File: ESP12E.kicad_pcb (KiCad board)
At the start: 2 copper layers, 100 x 100 mm, 55 parts, among them J3 UART, J4 Motor, J5 12v PWR, J6 Sol_1, J7 Sol_2, J8 Sol_3, J9 Sol_4, Q1 IRF520N, Q2 IRF520N, Q3 IRF520N, Q4 IRF520N, Q5 IRF520N, U1 ESP-12E, U2 LM7805_TO220, U3 AMS1117-3.3, U4 HX710(A/B), U5 MPS-2108, U6 MPS-2108, U7 HX710(A/B)

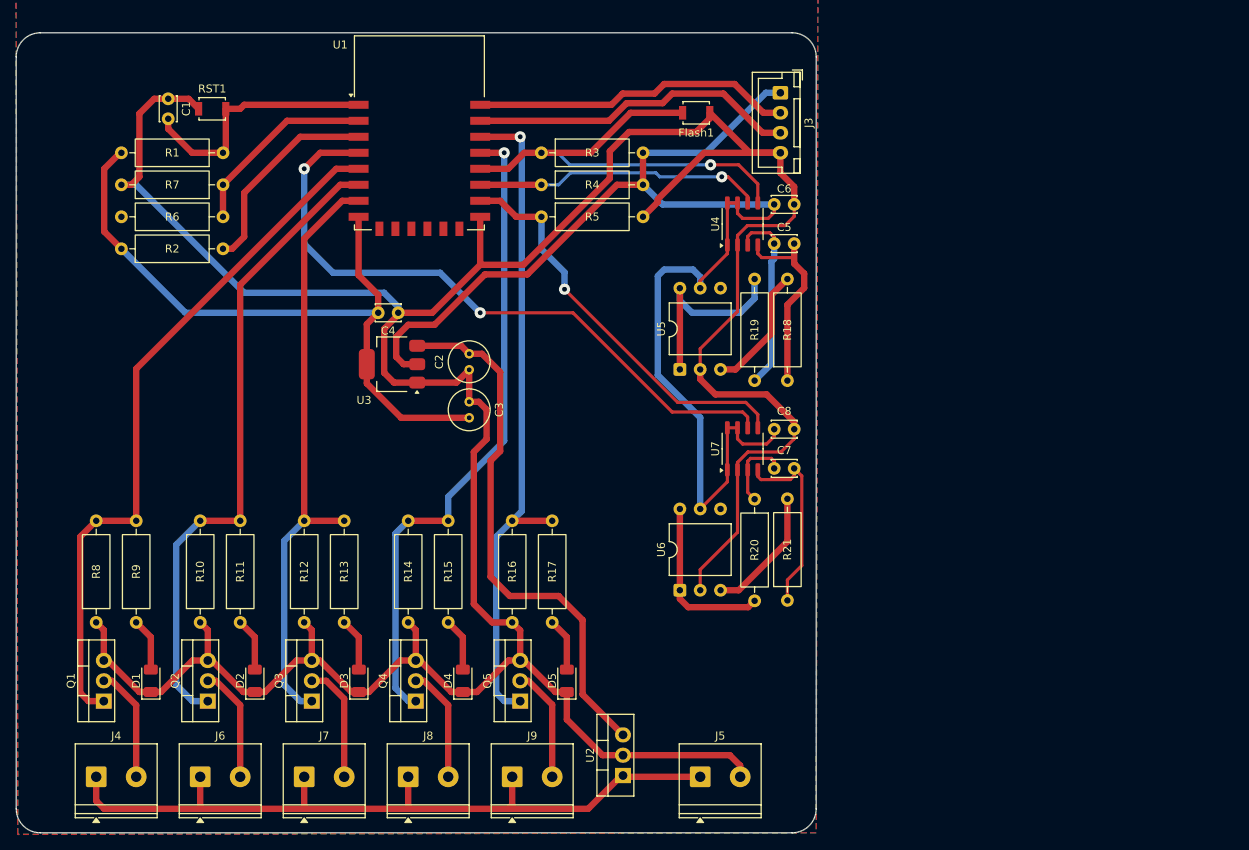
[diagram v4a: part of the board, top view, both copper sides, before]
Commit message: Feat: adding TLP250 for Isolation and driving MOSFETs.
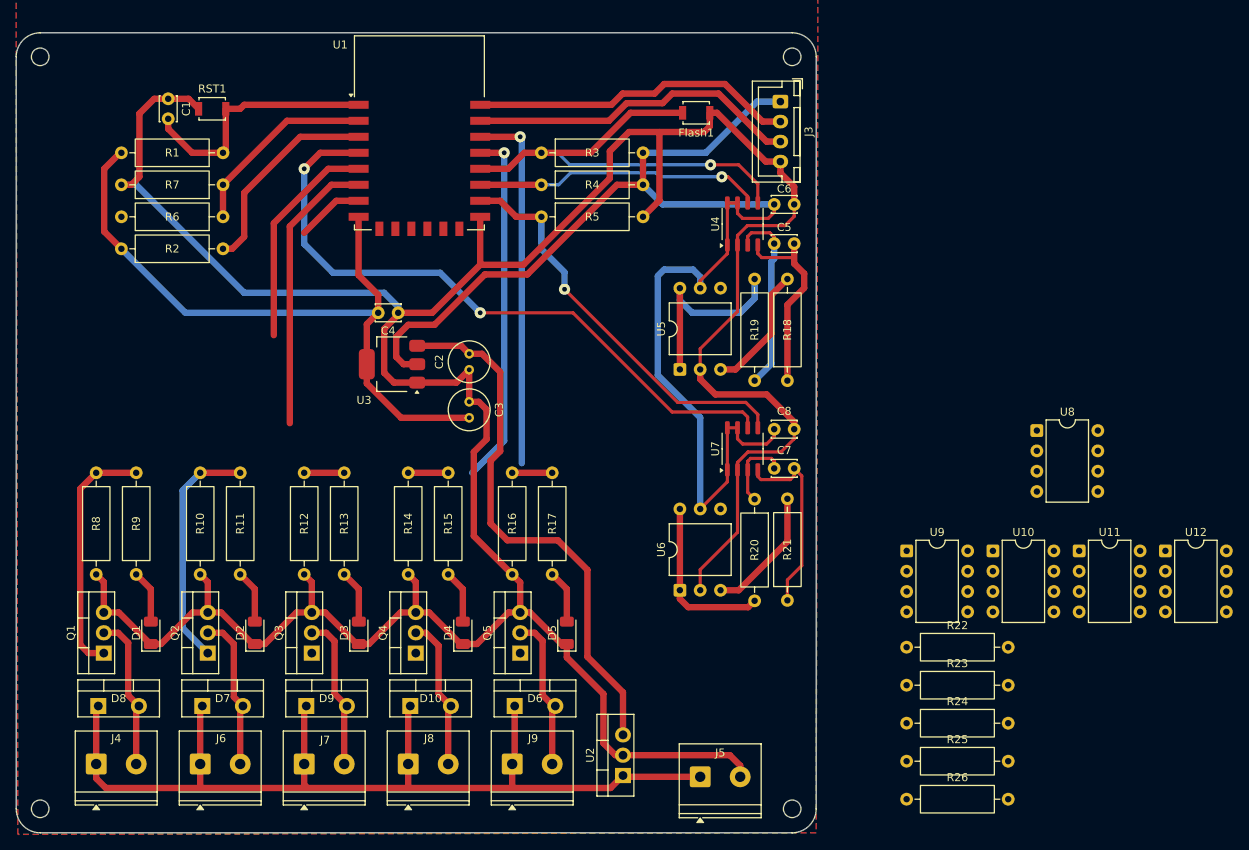
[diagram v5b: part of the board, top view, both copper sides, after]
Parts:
- added D10: MBR745, Package_TO_SOT_THT:TO-220-2_Vertical, F.Cu at (74.3, 104.2)
- added D6: MBR745, Package_TO_SOT_THT:TO-220-2_Vertical, F.Cu at (87.3, 104.2)
- added D7: MBR745, Package_TO_SOT_THT:TO-220-2_Vertical, F.Cu at (48.3, 104.2)
- added D8: MBR745, Package_TO_SOT_THT:TO-220-2_Vertical, F.Cu at (35.3, 104.2)
- added D9: MBR745, Package_TO_SOT_THT:TO-220-2_Vertical, F.Cu at (61.3, 104.2)
- added H1: MountingHole, MountingHole:MountingHole_2.2mm_M2, F.Cu at (122.0, 23.0)
- added H2: MountingHole, MountingHole:MountingHole_2.2mm_M2, F.Cu at (28.0, 23.0)
- added H3: MountingHole, MountingHole:MountingHole_2.2mm_M2, F.Cu at (28.0, 117.0)
- added H4: MountingHole, MountingHole:MountingHole_2.2mm_M2, F.Cu at (122.0, 117.0)
- added R22: 1k, Resistor_THT:R_Axial_DIN0309_L9.0mm_D3.2mm_P12.70mm_Horizontal, F.Cu at (136.3, 96.8)
- added R23: 1k, Resistor_THT:R_Axial_DIN0309_L9.0mm_D3.2mm_P12.70mm_Horizontal, F.Cu at (136.3, 101.5)
- added R24: 1k, Resistor_THT:R_Axial_DIN0309_L9.0mm_D3.2mm_P12.70mm_Horizontal, F.Cu at (136.3, 106.3)
- added R25: 1k, Resistor_THT:R_Axial_DIN0309_L9.0mm_D3.2mm_P12.70mm_Horizontal, F.Cu at (136.3, 111.0)
- added R26: 1k, Resistor_THT:R_Axial_DIN0309_L9.0mm_D3.2mm_P12.70mm_Horizontal, F.Cu at (136.3, 115.8)
- added U10: TLP250, Package_DIP:DIP-8_W7.62mm, F.Cu at (147.1, 84.8)
- added U11: TLP250, Package_DIP:DIP-8_W7.62mm, F.Cu at (157.9, 84.8)
- added U12: TLP250, Package_DIP:DIP-8_W7.62mm, F.Cu at (168.7, 84.8)
- added U8: TLP250, Package_DIP:DIP-8_W7.62mm, F.Cu at (152.6, 69.7)
- added U9: TLP250, Package_DIP:DIP-8_W7.62mm, F.Cu at (136.3, 84.8)
- moved D1 6.00 mm to (41.8, 95.0)
- moved D2 6.00 mm to (54.8, 95.0)
- moved D3 6.00 mm to (67.8, 95.0)
- moved D4 6.00 mm to (80.8, 95.0)
- moved D5 6.00 mm to (93.8, 95.0)
- moved Q1 6.00 mm to (36.0, 97.5)
- moved Q2 6.00 mm to (49.0, 97.5)
- moved Q3 6.00 mm to (62.0, 97.5)
- moved Q4 6.00 mm to (75.0, 97.5)
- moved Q5 6.00 mm to (88.0, 97.5)
- moved R10 6.00 mm to (48.0, 87.7)
- moved R11 6.00 mm to (53.0, 87.7)
- moved R12 6.00 mm to (61.0, 87.7)
- moved R13 6.00 mm to (66.0, 87.7)
- moved R14 6.00 mm to (74.0, 87.7)
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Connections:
- Q1 pad 1: D5/GPIO14/SCLK -> Net-(Q1-G)
- Q2 pad 1: D6/GPIO12/MISO -> Net-(Q2-G)
- Q3 pad 1: D7/GPIO13/MOSI -> Net-(Q3-G)
- Q4 pad 1: D2/SDA/GPIO4 -> Net-(Q4-G)
- Q5 pad 1: D1/SCL/GPIO5 -> Net-(Q5-G)
- R10 pad 2: D6/GPIO12/MISO -> Net-(Q2-G)
- R11 pad 2: D6/GPIO12/MISO -> Net-(Q2-G)
- R12 pad 2: D7/GPIO13/MOSI -> Net-(Q3-G)
- R13 pad 2: D7/GPIO13/MOSI -> Net-(Q3-G)
- R14 pad 2: D2/SDA/GPIO4 -> Net-(Q4-G)
- R15 pad 2: D2/SDA/GPIO4 -> Net-(Q4-G)
- R16 pad 2: D1/SCL/GPIO5 -> Net-(Q5-G)
- R17 pad 2: D1/SCL/GPIO5 -> Net-(Q5-G)
- R8 pad 2: D5/GPIO14/SCLK -> Net-(Q1-G)
- R9 pad 2: D5/GPIO14/SCLK -> Net-(Q1-G)
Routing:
- net D7/GPIO13/MOSI: track 74.8 -> 8.46 mm
- net D5/GPIO14/SCLK: track 87.9 -> 27.4 mm
- net D6/GPIO12/MISO: track 81.0 -> 35.4 mm
- net D1/SCL/GPIO5: track 84.3 -> 45.9 mm
- net D2/SDA/GPIO4: track 81.7 -> 44.7 mm
- net +12V: track 96.8 -> 127.6 mm
- net Net-(Q1-G): track 0.00 -> 30.7 mm
- net Net-(Q2-G): track 0.00 -> 29.8 mm
- net GND: track 413.9 -> 402.2 mm
- net Net-(D6-A): track 14.3 -> 19.6 mm
- net Net-(D7-A): track 14.3 -> 19.4 mm
- net Net-(D8-A): track 14.3 -> 19.4 mm
- net Net-(Q5-G): track 0.00 -> 5.00 mm
- net Net-(Q4-G): track 0.00 -> 5.00 mm
- net Net-(Q3-G): track 0.00 -> 5.00 mm
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
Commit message: working: continue at Work.
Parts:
- J4, J5, J6, J7, J8, J9: footprint TerminalBlock_Phoenix:TerminalBlock_Phoenix_PT-1,5-2-5.0-H_1x02_P5.00mm_Horizontal -> TerminalBlock_RND:TerminalBlock_RND_205-00276_1x02_P5.00mm_Vertical
- R1, R10, R11, R12, R13, R14, R15, R16, R17, R18, R19, R2, R20, R21, R22, R23, R24, R25, R26, R3, R4, R5, R6, R7, R8, R9: footprint Resistor_THT:R_Axial_DIN0309_L9.0mm_D3.2mm_P12.70mm_Horizontal -> Resistor_SMD:R_1206_3216Metric_Pad1.30x1.75mm_HandSolder
- moved U12 135.3 mm to (33.6, 76.6)
- moved R26 112.5 mm to (30.6, 77.5), turned to 90 degrees
- moved U11 111.6 mm to (46.6, 76.6)
- moved R25 98.2 mm to (44.0, 77.5), turned to 90 degrees
- moved U10 87.9 mm to (59.6, 76.6)
- moved R24 84.4 mm to (57.0, 77.5), turned to 90 degrees
- moved R23 70.6 mm to (70.0, 77.5), turned to 90 degrees
- moved U8 67.3 mm to (85.6, 76.6)
- moved U9 64.3 mm to (72.6, 76.6)
- moved R22 56.7 mm to (83.0, 77.5), turned to 90 degrees
- moved Flash1 22.0 mm to (89.2, 37.2)
- moved J3 19.5 mm to (101.8, 23.0), turned to 0 degrees
- moved R2 15.3 mm to (53.5, 31.9), turned to 90 degrees
- moved R18 15.3 mm to (122.4, 48.2)
- moved R19 15.3 mm to (118.3, 48.2)
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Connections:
- J3 pad 1: +3.3V -> TX
- J3 pad 2: TX -> RX
- J3 pad 3: RX -> +3.3V
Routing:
- net +12V: track 127.6 -> 293.7 mm
- net +3.3V: track 251.6 -> 112.8 mm, vias 0 -> 2
- net D0/GPIO16: track 82.9 -> 3.20 mm, vias 2 -> 1
- net D3/GPIO0: track 59.2 -> 8.60 mm, vias 1 -> 0
- net D8/GPIO15/SS: track 51.0 -> 4.66 mm, vias 1 -> 0
- net GND: track 402.2 -> 369.2 mm, vias 0 -> 1
- net D7/GPIO13/MOSI: track 8.46 -> 41.1 mm
- net D4/GPIO2: track 36.1 -> 5.31 mm, vias 1 -> 0
- net D5/GPIO14/SCLK: track 27.4 -> 56.0 mm
- net Net-(U4-INP): track 26.1 -> 0.00 mm
- net Net-(R19-Pad2): track 24.8 -> 0.00 mm
- net Net-(U7-INP): track 24.3 -> 0.00 mm
- net Net-(U4-INN): track 23.7 -> 0.00 mm
- net Net-(R20-Pad2): track 21.3 -> 0.00 mm
- net TX: track 40.5 -> 23.4 mm
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
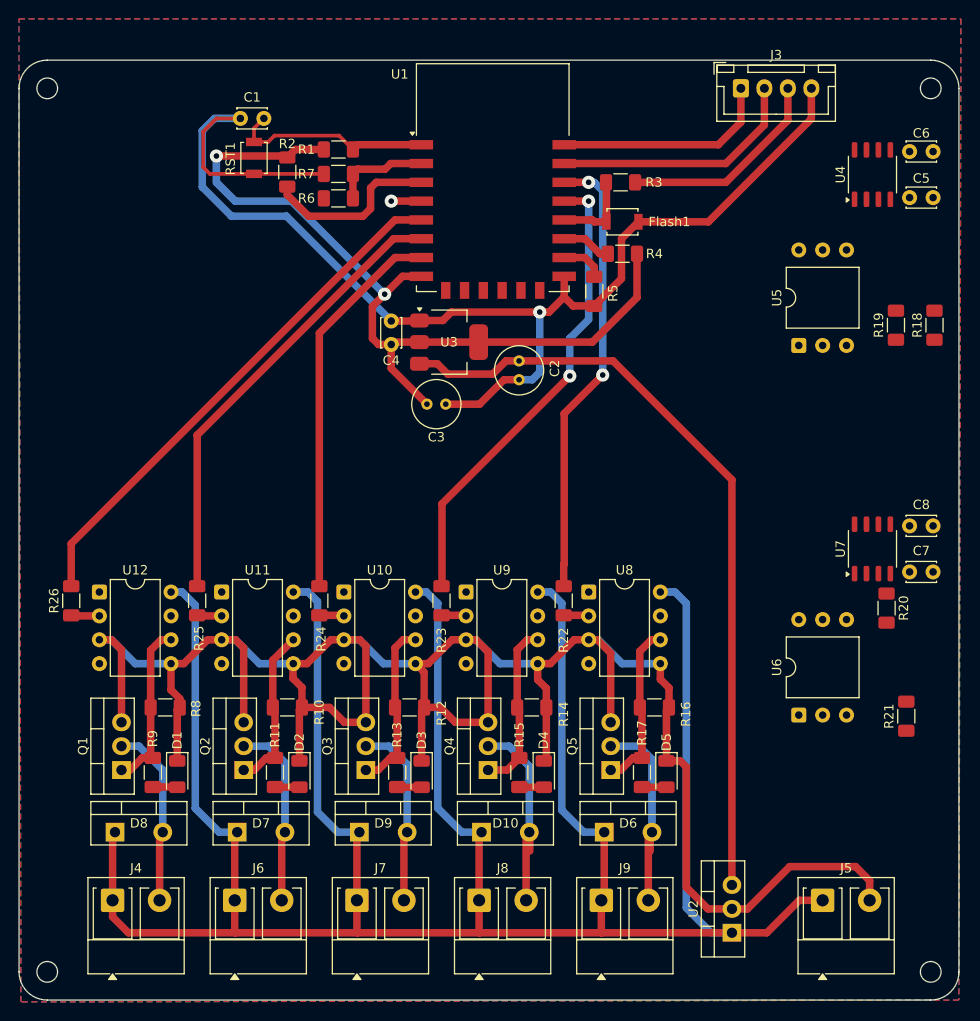
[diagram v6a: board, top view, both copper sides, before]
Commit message: Feat: adding Buck converter + making BOM files HTML with LINKs of stores + small edits + adding polarity protection.
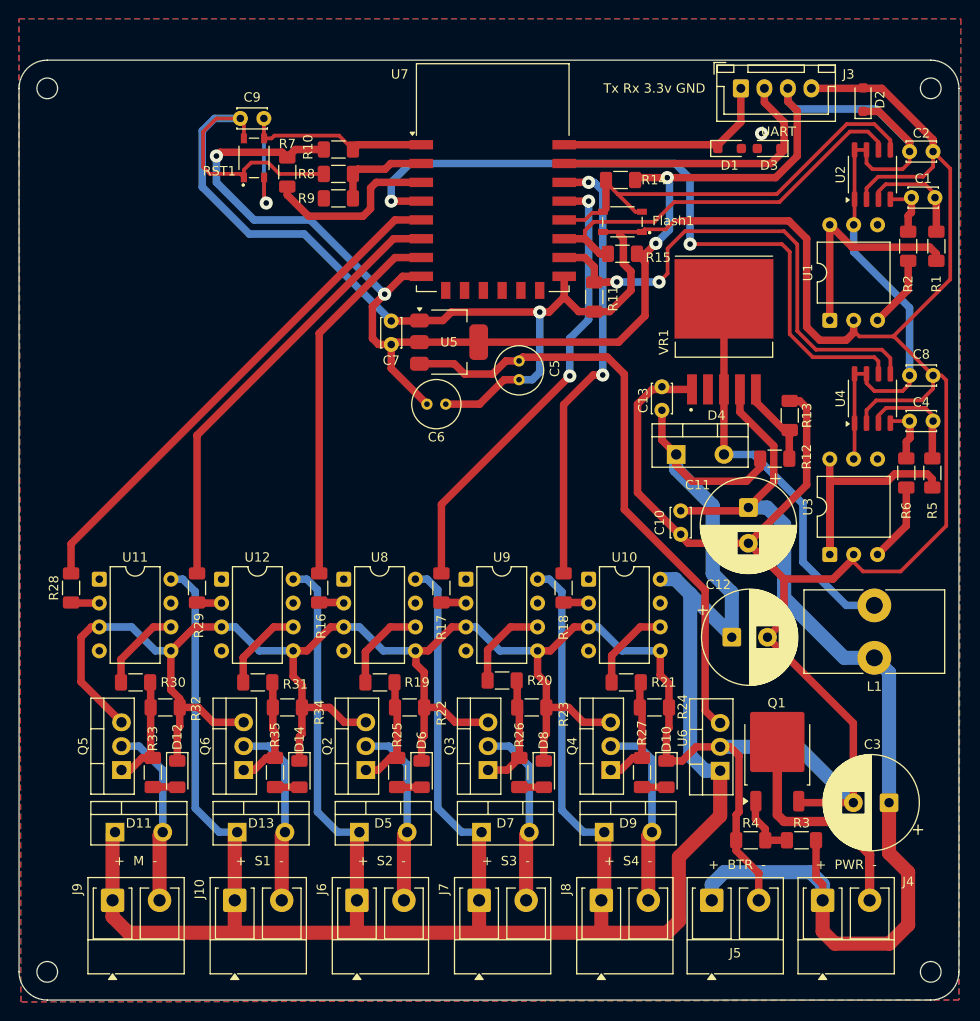
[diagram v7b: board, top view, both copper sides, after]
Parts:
- added C10: 100nF, Capacitor_THT:C_Disc_D3.0mm_W2.0mm_P2.50mm, F.Cu at (95.4, 70.5)
- added C11: 220uF/16V, Capacitor_THT:CP_Radial_D10.0mm_P3.80mm, F.Cu at (102.6, 67.6)
- added C12: 220uF/16V, Capacitor_THT:CP_Radial_D10.0mm_P3.80mm, F.Cu at (100.8, 81.4)
- added C13: 100nF, Capacitor_THT:C_Disc_D3.0mm_W2.0mm_P2.50mm, F.Cu at (93.4, 54.8)
- added C3: 470uF/16V, Capacitor_THT:CP_Radial_D10.0mm_P3.80mm, F.Cu at (117.6, 99.0)
- added D1: CESD5V0D3, Diode_SMD:D_SOD-323_HandSoldering, F.Cu at (100.6, 29.4)
- added D2: CESD5V0D3, Diode_SMD:D_SOD-323_HandSoldering, F.Cu at (114.8, 24.2)
- added D3: CESD5V0D3, Diode_SMD:D_SOD-323_HandSoldering, F.Cu at (104.8, 29.4)
- added D4: MBR745, Package_TO_SOT_THT:TO-220-2_Vertical, F.Cu at (94.9, 62.0)
- added J5: Battery, TerminalBlock_RND:TerminalBlock_RND_205-00276_1x02_P5.00mm_Vertical, F.Cu at (98.7, 109.4)
- added L1: 47uH, Inductor_THT:L_Toroid_Vertical_L14.7mm_W8.6mm_P5.58mm_Pulse_KM-1, F.Cu at (116.0, 83.6)
- added Q1: RU3560L, Package_TO_SOT_SMD:TO-252-2, F.Cu at (105.7, 93.8)
- added R12: 30k, Resistor_SMD:R_1206_3216Metric_Pad1.30x1.75mm_HandSolder, F.Cu at (105.4, 62.4)
- added R13: 3k3, Resistor_SMD:R_1206_3216Metric_Pad1.30x1.75mm_HandSolder, F.Cu at (107.0, 57.8)
- added R19: 15, Resistor_SMD:R_1206_3216Metric_Pad1.30x1.75mm_HandSolder, F.Cu at (63.4, 86.2)
- added R20: 15, Resistor_SMD:R_1206_3216Metric_Pad1.30x1.75mm_HandSolder, F.Cu at (76.4, 86.0)
- added R21: 15, Resistor_SMD:R_1206_3216Metric_Pad1.30x1.75mm_HandSolder, F.Cu at (89.6, 86.2)
- added R3: 47, Resistor_SMD:R_1206_3216Metric_Pad1.30x1.75mm_HandSolder, F.Cu at (108.2, 103.0)
- added R30: 15, Resistor_SMD:R_1206_3216Metric_Pad1.30x1.75mm_HandSolder, F.Cu at (37.4, 86.2)
- added R31: 15, Resistor_SMD:R_1206_3216Metric_Pad1.30x1.75mm_HandSolder, F.Cu at (50.4, 86.2)
- added R4: 4k7, Resistor_SMD:R_1206_3216Metric_Pad1.30x1.75mm_HandSolder, F.Cu at (102.8, 103.0)
- added VR1: XL6019E1, Converter_DCDC:TO-263-5, F.Cu at (100.0, 48.9)
- Flash1, RST1: footprint Button_Switch_SMD:SW_SPST_B3U-1000P -> Button_Switch_SMD:SW_SKRPACE010
- Q2: renamed from Q3; value IRF520N -> IRF540N
- Q3: renamed from Q4; value IRF520N -> IRF540N
- Q4: renamed from Q5; value IRF520N -> IRF540N
- Q5: renamed from Q1; value IRF520N -> IRF540N
- Q6: renamed from Q2; value IRF520N -> IRF540N
- moved R6 25.9 mm to (119.4, 63.9), turned to -90 degrees
- moved U3 17.4 mm to (111.3, 72.6)
- moved U6 17.3 mm to (99.6, 95.6)
- moved C4 16.2 mm to (122.2, 58.4), turned to 180 degrees
- moved C8 16.0 mm to (119.8, 53.5)
- moved U4 16.0 mm to (115.8, 56.0)
- moved R5 15.2 mm to (122.2, 63.9)
- moved R1 9.44 mm to (122.6, 39.8), turned to -90 degrees
- moved R2 8.85 mm to (119.6, 39.8), turned to -90 degrees
- moved U1 4.25 mm to (111.3, 47.7)
- moved C1 2.70 mm to (122.5, 34.6), turned to 180 degrees
- moved R16 1.36 mm to (56.9, 76.2)
- moved R17 1.36 mm to (69.9, 76.2)
- moved R18 1.36 mm to (82.9, 76.2)
- moved R28 1.36 mm to (30.5, 76.2)
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- renumbered C5 to C1, C6 to C2, C7 to C4, C2 to C5, C3 to C6, C4 to C7, C1 to C9, D5 to D10, D8 to D11, D1 to D12, D7 to D13, D2 to D14, D9 to D5, D3 to D6, D10 to D7, D4 to D8, D6 to D9, J6 to J10, J5 to J4, J7 to J6, J8 to J7, J9 to J8, J4 to J9, R19 to R1, R1 to R10, R5 to R11, R3 to R14, R4 to R15, R24 to R16, R23 to R17, R22 to R18, R18 to R2, R12 to R22, R14 to R23, R16 to R24, R13 to R25, R15 to R26, R17 to R27, R26 to R28, R25 to R29, R8 to R32, R9 to R33, R10 to R34, R11 to R35, R20 to R5, R21 to R6, R2 to R7, R7 to R8, R6 to R9, U5 to U1, U8 to U10, U12 to U11, U11 to U12, U4 to U2, U6 to U3, U7 to U4, U3 to U5, U2 to U6, U1 to U7, U10 to U8
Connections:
- J4 pad 1: +12V -> V_btr
- J4 pad 2: GND -> Net-(J4-Pin_2)
- Q2 pad 1: Net-(Q3-G) -> Net-(Q2-G)
- Q3 pad 1: Net-(Q4-G) -> Net-(Q3-G)
- Q4 pad 1: Net-(Q5-G) -> Net-(Q4-G)
- Q5 pad 1: Net-(Q1-G) -> Net-(Q5-G)
- Q6 pad 1: Net-(Q2-G) -> Net-(Q6-G)
- R22 pad 2: Net-(Q3-G) -> Net-(Q2-G)
- R23 pad 2: Net-(Q4-G) -> Net-(Q3-G)
- R24 pad 2: Net-(Q5-G) -> Net-(Q4-G)
- R25 pad 2: Net-(Q3-G) -> Net-(Q2-G)
- R26 pad 2: Net-(Q4-G) -> Net-(Q3-G)
- R27 pad 2: Net-(Q5-G) -> Net-(Q4-G)
- R32 pad 2: Net-(Q1-G) -> Net-(Q5-G)
- R33 pad 2: Net-(Q1-G) -> Net-(Q5-G)
- R34 pad 2: Net-(Q2-G) -> Net-(Q6-G)
- R35 pad 2: Net-(Q2-G) -> Net-(Q6-G)
- U10 pad 6: Net-(Q5-G) -> Net-(R21-Pad1)
- U11 pad 6: Net-(Q1-G) -> Net-(R30-Pad1)
- U12 pad 6: Net-(Q2-G) -> Net-(R31-Pad1)
- U8 pad 6: Net-(Q3-G) -> Net-(R19-Pad1)
- U9 pad 6: Net-(Q4-G) -> Net-(R20-Pad1)
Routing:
- net GND: track 369.2 -> 572.5 mm, vias 1 -> 2
- net V_btr: track 0.00 -> 113.7 mm
- net +3.3V: track 112.8 -> 206.6 mm, vias 2 -> 4
- net D0/GPIO16: track 3.20 -> 77.1 mm, vias 1 -> 2
- net D8/GPIO15/SS: track 4.66 -> 53.2 mm, vias 0 -> 2
- net Net-(D4-A): track 0.00 -> 42.8 mm
- net +12V: track 293.7 -> 332.0 mm
- net D3/GPIO0: track 8.60 -> 46.6 mm
- net D4/GPIO2: track 5.31 -> 43.1 mm
- net Net-(R5-Pad2): track 0.00 -> 30.3 mm
- net Net-(J4-Pin_2): track 0.00 -> 24.2 mm
- net Net-(R1-Pad2): track 0.00 -> 23.5 mm
- net +5V: track 82.6 -> 65.3 mm
- net Net-(Q6-G): track 0.00 -> 12.3 mm
- net Net-(U4-INN): track 0.00 -> 11.9 mm
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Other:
- board text added: "+ BTR -"
- board text added: "+ M -"
- board text added: "+ PWR -"
- board text added: "+ S1 -"
- board text added: "+ S2 -"
- board text added: "+ S3 -"
- board text added: "+ S4 -"
- board text added: "Tx Rx 3.3v GND"
- board text added: "UART"

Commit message: Fix: edit pcb for manufacturing Bad process (local manufacturing).
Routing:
- net GND: track 572.5 -> 591.1 mm, vias 2 -> 6
- net V_btr: track 113.7 -> 119.7 mm, vias 0 -> 1
- net Net-(Q5-G): track 12.0 -> 16.4 mm, vias 0 -> 1
- net Net-(Q4-G): track 12.0 -> 16.3 mm, vias 0 -> 1
- net Net-(Q2-G): track 12.0 -> 16.1 mm, vias 0 -> 1
- net Net-(Q3-G): track 12.2 -> 16.2 mm, vias 0 -> 1
- net +3.3V: track 206.6 -> 202.7 mm, vias 4 -> 6
- net Net-(Q6-G): track 12.3 -> 16.2 mm, vias 0 -> 1
- net Net-(R5-Pad2): track 30.3 -> 27.2 mm, vias 0 -> 1
- net +12V: track 332.0 -> 334.3 mm, vias 0 -> 5
- net TX: track 23.4 -> 24.6 mm, vias 0 -> 1
- net RX: track 31.4 -> 32.4 mm, vias 0 -> 1
- net Net-(U3-Vo+): vias 0 -> 1
- net Net-(J4-Pin_2): vias 0 -> 1
